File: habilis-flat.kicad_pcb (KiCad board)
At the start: 2 copper layers, 164.5 x 172.8 mm, 74 parts, among them SW1 MX, SW10 MX, SW11 MX, SW12 MX, SW13 MX, SW14 MX, SW15 MX, SW16 MX, SW17 MX, SW18 MX, SW19 MX, SW2 MX, SW20 MX, SW21 MX, SW22 MX, SW23 MX, SW24 MX, SW25 MX, SW26 MX, SW27 MX, SW28 MX, SW29 MX, SW3 MX, SW30 MX, SW31 MX, SW32 MX, SW33 MX, SW34 MX, SW35 MX, SW4 MX, SW5 MX, SW6 MX, SW7 MX, SW8 MX, SW9 MX, U1 ProMicro

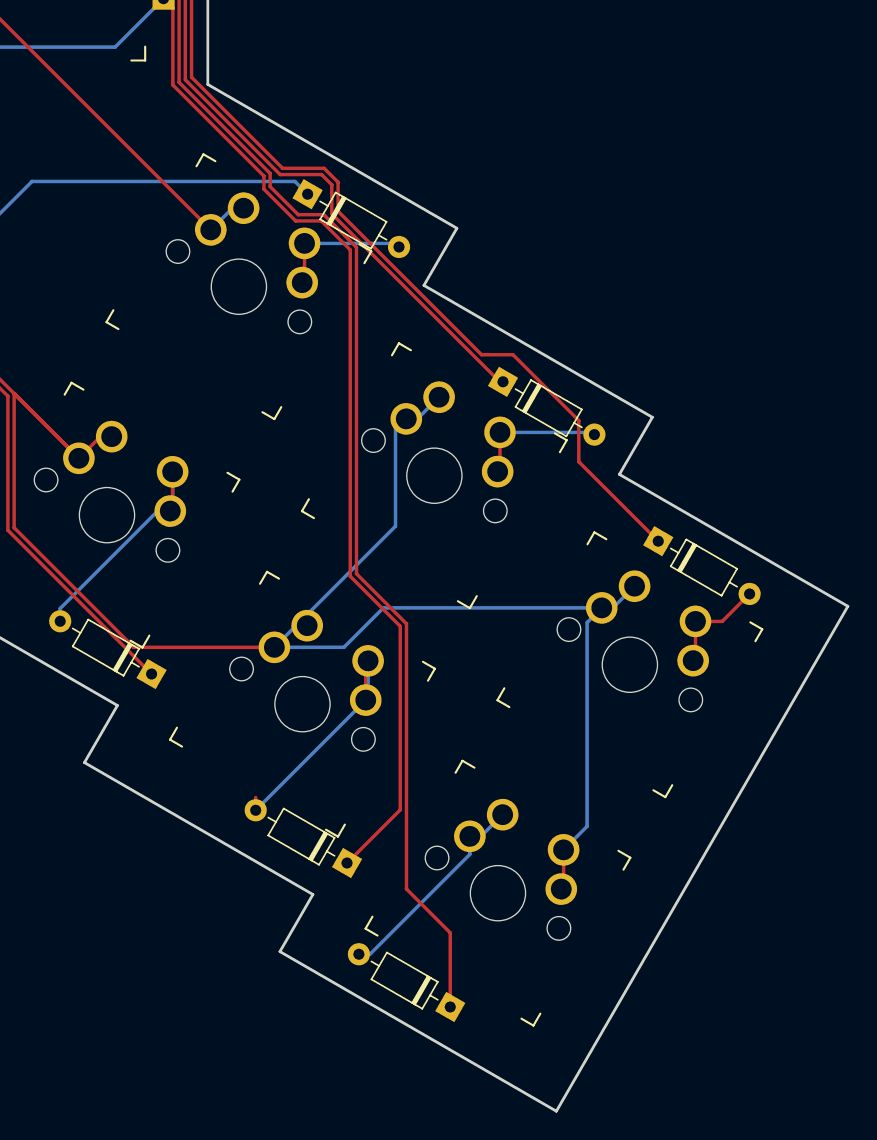
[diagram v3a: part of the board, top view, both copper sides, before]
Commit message: Make board a bit less sharp
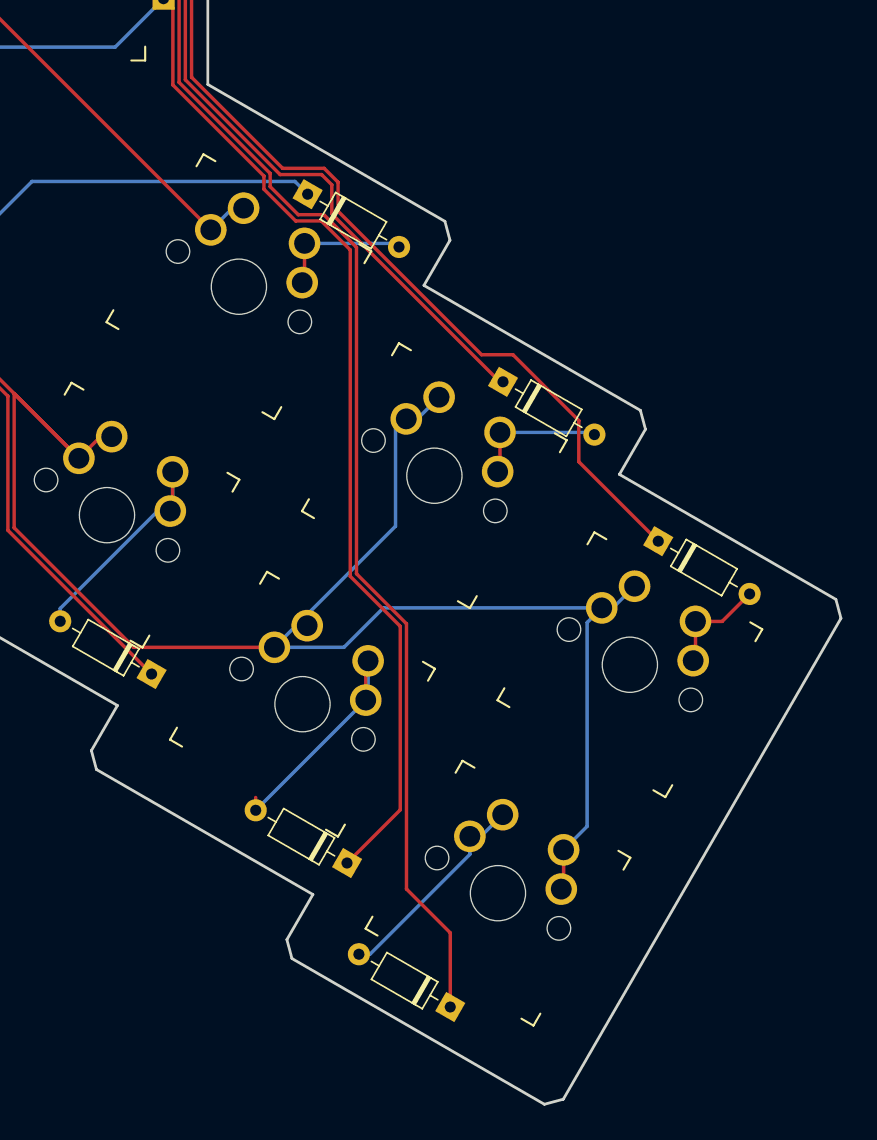
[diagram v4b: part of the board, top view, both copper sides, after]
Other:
- board size 164.5 x 172.8 mm -> 164 x 172.3 mm
